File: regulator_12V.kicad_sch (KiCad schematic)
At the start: 4 parts, among them U34 LT3045IDD

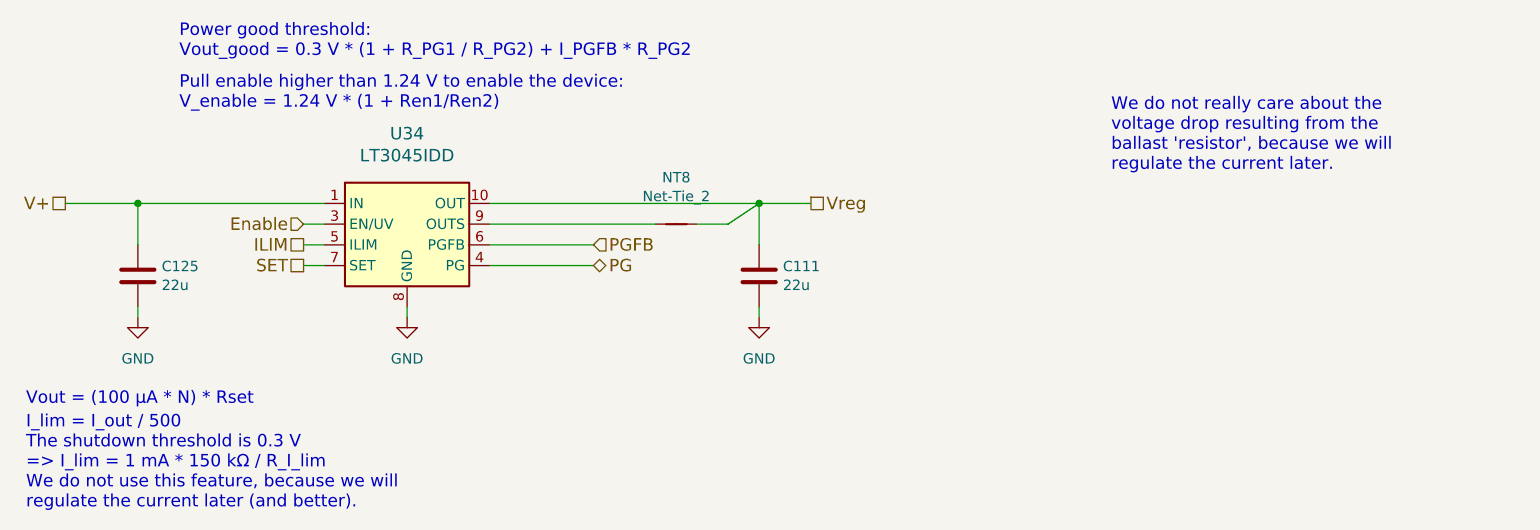
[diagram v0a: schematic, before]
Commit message: Added M3 mounting holes (#9)
- fixed custom library footprint link
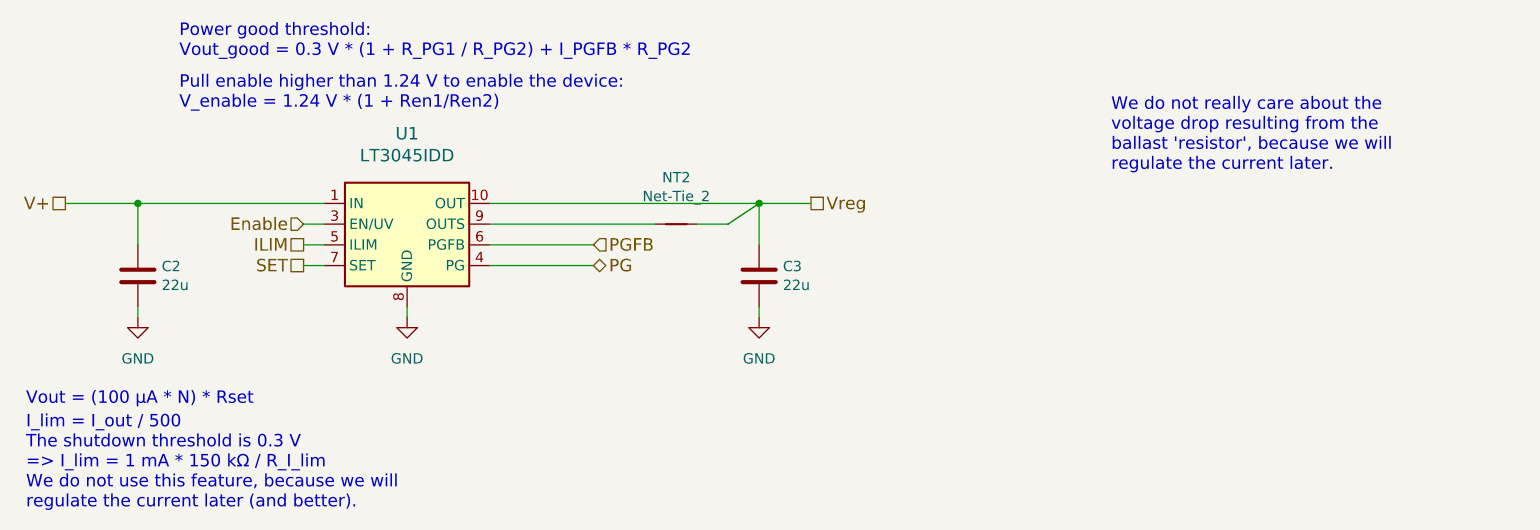
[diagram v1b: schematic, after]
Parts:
- NT2: renamed from NT8; footprint Custom:NetTie-2_SMD_Pad0.2mm -> Custom_footprints_project:NetTie-2_SMD_Pad0.2mm
- renumbered C125 to C2, C111 to C3, U34 to U1
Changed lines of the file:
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@@
 		(on_board yes)
 		(dnp no)
-		(property "Reference" "C125"
+		(property "Reference" "C2"
 			(at 112.141 57.2516 0)
 			(effects
@@
 			(project "ocxo_breakout"
 				(path "/b550b6dd-f44b-4072-aec4-12b3a5ef6ae2/ff411146-2dd4-4703-8d6a-224a0f2e5e43"
-					(reference "C125")
+					(reference "C2")
 					(unit 1)
 				)
@@
 		(on_board yes)
 		(dnp no)
-		(property "Reference" "C111"
+		(property "Reference" "C3"
 			(at 188.341 57.2516 0)
 			(effects
@@
 			(project "ocxo_breakout"
 				(path "/b550b6dd-f44b-4072-aec4-12b3a5ef6ae2/ff411146-2dd4-4703-8d6a-224a0f2e5e43"
-					(reference "C111")
+					(reference "C3")
 					(unit 1)
 				)
@@
 		(on_board yes)
 		(dnp no)
-		(property "Reference" "NT8"
+		(property "Reference" "NT2"
 			(at 175.26 46.355 0)
 			(effects
@@
 			)
 		)
-		(property "Footprint" "Custom:NetTie-2_SMD_Pad0.2mm"
+		(property "Footprint" "Custom_footprints_project:NetTie-2_SMD_Pad0.2mm"
 			(at 175.26 52.07 0)
 			(effects
@@
 			(project "ocxo_breakout"
 				(path "/b550b6dd-f44b-4072-aec4-12b3a5ef6ae2/ff411146-2dd4-4703-8d6a-224a0f2e5e43"
-					(reference "NT8")
+					(reference "NT2")
 					(unit 1)
 				)
@@
 		(on_board yes)
 		(dnp no)
-		(property "Reference" "U34"
+		(property "Reference" "U1"
 			(at 142.24 40.9702 0)
 			(effects
@@
 			(project "ocxo_breakout"
 				(path "/b550b6dd-f44b-4072-aec4-12b3a5ef6ae2/ff411146-2dd4-4703-8d6a-224a0f2e5e43"
-					(reference "U34")
+					(reference "U1")
 					(unit 1)
 				)

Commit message: Added missing part values (#10)
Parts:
- U1: Alternative (none) -> Analog Devices LT3045IDD#TRPBF
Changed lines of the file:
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@@
+			)
+		)
+		(property "Alternative" "Analog Devices LT3045IDD#TRPBF"
+			(at 142.24 52.07 0)
+			(effects
+				(font
+					(size 1.27 1.27)
+				)
+				(hide yes)
 			)
 		)
